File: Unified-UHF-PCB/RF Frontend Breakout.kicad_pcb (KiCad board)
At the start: 2 copper layers, 82.5 x 82.5 mm, 74 parts, among them IC1 QPC1022SR, IC2 GRF5504, IC3 LHA-13LN+, IC4 QPC1022SR, J2 Conn_01x02, J3 Conn_01x02, J4 Conn_Coaxial, J5 Conn_01x05, J6 Conn_01x02, U1 AT86RF215-ZU, U3 NCS-62+, X1 TYETACSANF-26.000000

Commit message: saving first
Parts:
- moved G*** 1.20 mm to (104.0, 91.9)
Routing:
- net +5V: track 138.7 -> 132.8 mm
- net Net-(FL2-RF_IN): track 13.4 -> 8.46 mm
- net Net-(IC4-RF1): track 27.5 -> 26.6 mm
- net Net-(FL2-RF_OUT): track 24.1 -> 23.5 mm
- net GND: track 133.7 -> 133.4 mm, vias 117 -> 1072

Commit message: small fixes
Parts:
- moved TP9 6.66 mm to (103.0, 62.4)
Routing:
- net Net-(IC4-ANT): track 11.1 -> 16.8 mm
- net GND: track 133.4 -> 136.2 mm, vias 1072 -> 1063
- net Net-(FL2-RF_IN): track 8.46 -> 7.55 mm
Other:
- board text added: "TP4"
- board text removed: "C1"

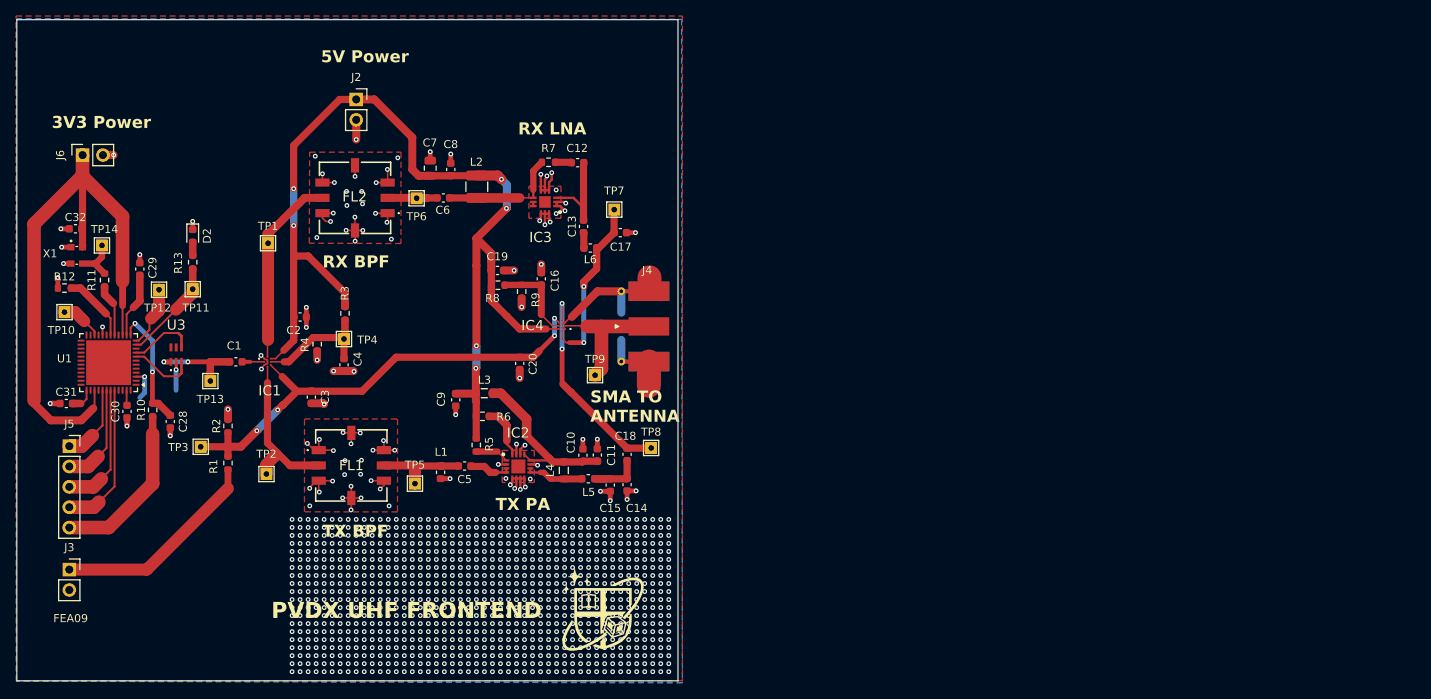
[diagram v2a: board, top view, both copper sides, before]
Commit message: mounting holes + design checker fixes
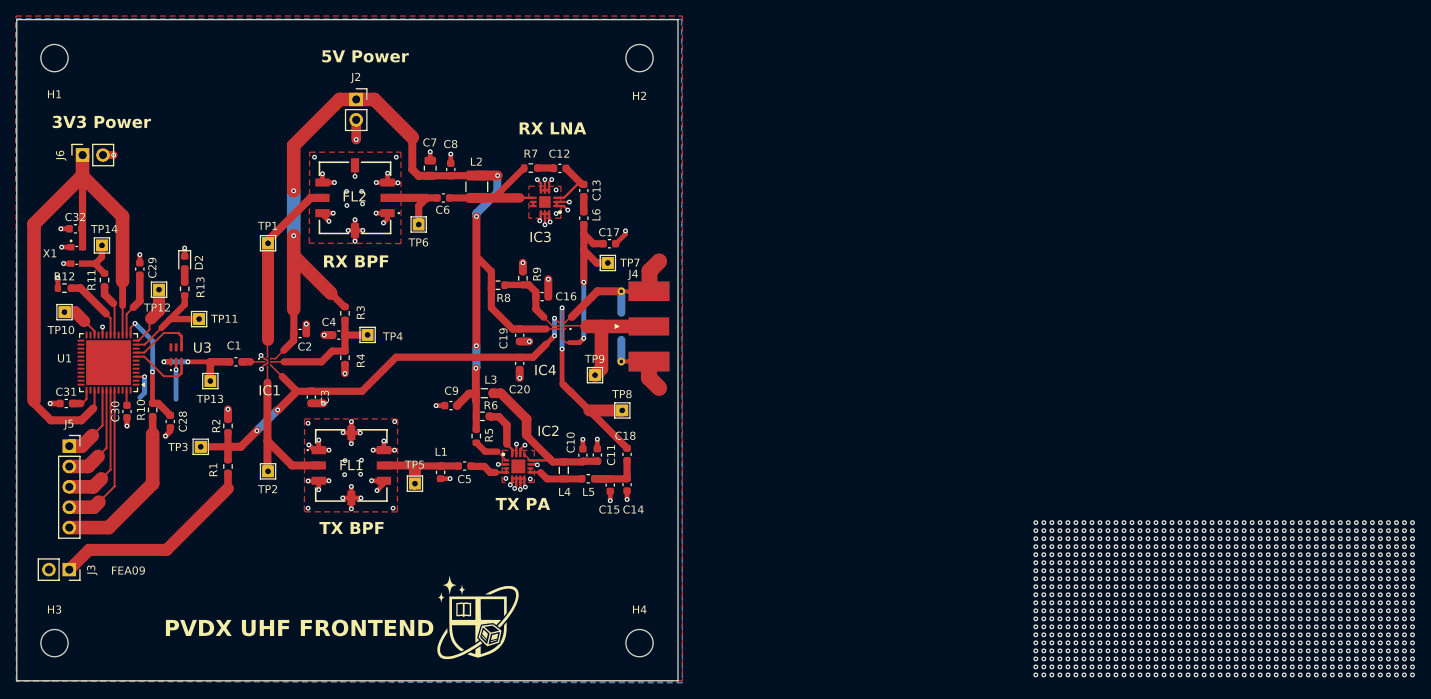
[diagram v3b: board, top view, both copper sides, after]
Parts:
- added H1: MountingHole, MountingHole:MountingHole_3.2mm_M3, F.Cu at (35.6, 22.8)
- added H2: MountingHole, MountingHole:MountingHole_3.2mm_M3, F.Cu at (108.6, 22.8)
- added H3: MountingHole, MountingHole:MountingHole_3.2mm_M3, F.Cu at (35.6, 95.8)
- added H4: MountingHole, MountingHole:MountingHole_3.2mm_M3, F.Cu at (108.6, 95.8)
- moved G*** 15.6 mm to (88.4, 93.0)
- moved C19 8.55 mm to (93.6, 57.4), turned to -90 degrees
- moved TP7 6.71 mm to (104.6, 48.4)
- moved TP8 5.91 mm to (106.4, 66.8)
- moved C13 4.47 mm to (101.6, 39.4)
- moved R4 3.86 mm to (71.8, 60.2)
- moved L6 3.81 mm to (101.6, 42.8), turned to 90 degrees
- moved TP11 3.81 mm to (53.6, 55.4)
- moved C4 3.77 mm to (71.0, 57.4), turned to 180 degrees
- moved D2 3.47 mm to (51.8, 48.4)
- moved R13 3.47 mm to (51.8, 51.6)
- moved TP6 3.28 mm to (81.0, 43.6)
- moved TP4 2.99 mm to (74.6, 57.4)
- moved C12 2.32 mm to (98.6, 36.6)
- moved R7 2.32 mm to (95.0, 36.5)
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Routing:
- net +5V: track 132.8 -> 125.8 mm
- net Net-(IC3-RF-IN): track 11.1 -> 6.89 mm
- net Net-(IC4-RF2): track 22.2 -> 24.9 mm
- net Net-(FL2-RF_IN): track 7.55 -> 10.0 mm
- net GND: track 136.2 -> 137.7 mm, vias 1063 -> 1061
- net Net-(IC1-EN): track 15.6 -> 16.7 mm
- net Net-(IC1-CTRL): track 61.6 -> 60.9 mm
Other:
- board text removed: "SMA TO ANTENNA"

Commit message: added via overlay
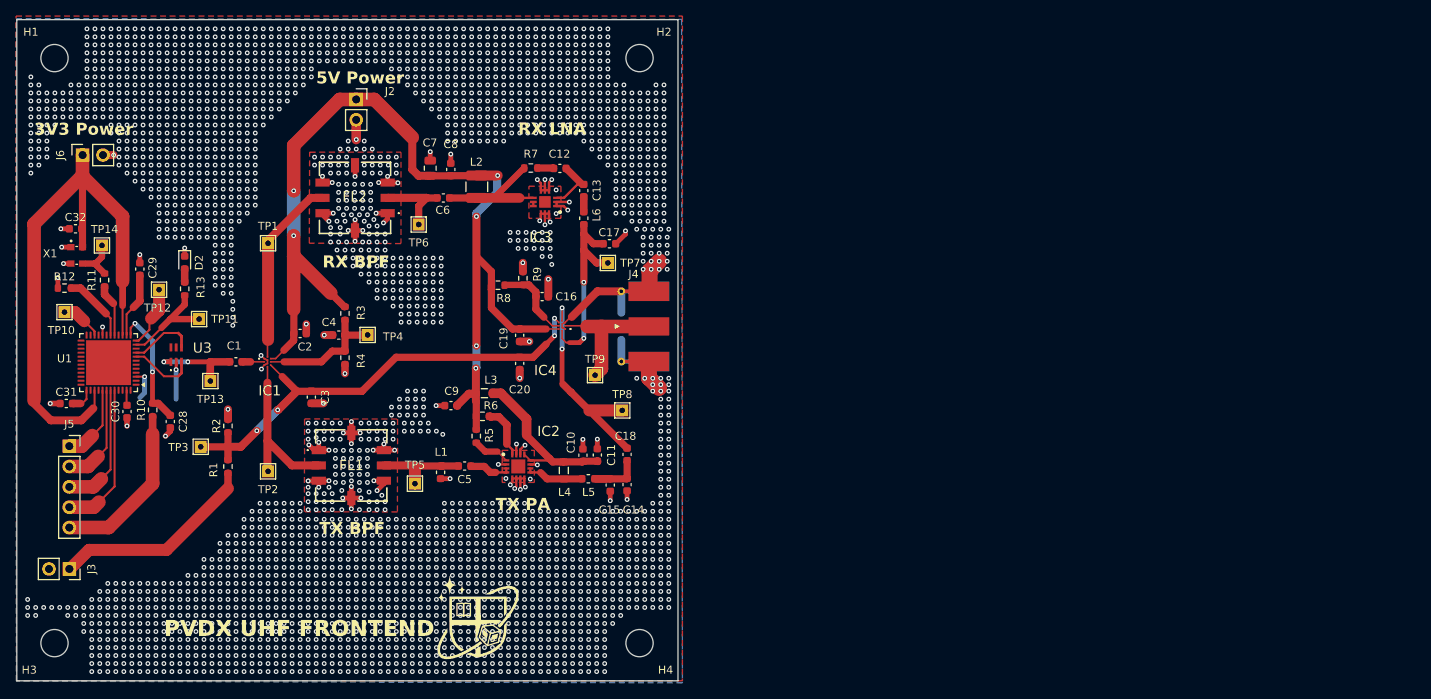
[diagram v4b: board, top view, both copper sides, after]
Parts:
- moved J3 0.09 mm to (37.4, 86.6)
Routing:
- net GND: track 137.7 -> 134.8 mm, vias 1061 -> 2963
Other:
- board text removed: "FEA09"

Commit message: fixed PA traces
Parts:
- moved C9 7.31 mm to (92.1, 64.2), turned to -90 degrees
- moved L3 6.57 mm to (94.6, 68.4), turned to -90 degrees
- moved C10 6.21 mm to (97.8, 67.4), turned to 0 degrees
- moved C11 6.12 mm to (97.8, 69.6), turned to 0 degrees
- moved C15 2.10 mm to (107.0, 76.2)
- moved C14 2.00 mm to (105.0, 76.1)
- moved C18 0.60 mm to (107.6, 72.3)
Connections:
- C10 pad 1: Net-(IC2-BIAS) -> +5V
- C11 pad 1: Net-(IC2-BIAS) -> +5V
- IC2 pad 12: Net-(IC2-BIAS) -> +5V
- IC2 pad 13: Net-(IC2-BIAS) -> Net-(IC2-VCC1)
- L3 pad 2: Net-(IC2-BIAS) -> Net-(IC2-VCC1)
- L4 pad 1: Net-(IC2-BIAS) -> +5V
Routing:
- net Net-(IC2-BIAS): track 21.6 -> 0.00 mm
- net +5V: track 125.8 -> 144.8 mm
- net Net-(IC2-VCC1): track 0.00 -> 3.08 mm
- net Net-(IC4-RF1): track 26.7 -> 27.2 mm

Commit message: fixed schematic as well
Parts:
- C2: value 100n -> 2.2n
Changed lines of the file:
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@@
 			)
 		)
-		(property "Value" "100n"
+		(property "Value" "2.2n"
 			(at 0 1.43 0)
 			(layer "F.Fab")
@@
 		(tags "capacitor")
 		(property "Reference" "C15"
-			(at 3.088291 0.1 180)
+			(at 3.088291 0.1 0)
 			(layer "F.SilkS")
 			(effects
